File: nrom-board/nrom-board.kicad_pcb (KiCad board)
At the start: 2 copper layers, 90 x 56.8 mm, 12 parts, among them J1 Cartridge Connector, SW1 SW_DIP_x04, SW2 SW_SPDT, U1 PRG ROM 512K, U2 CHR ROM 512K

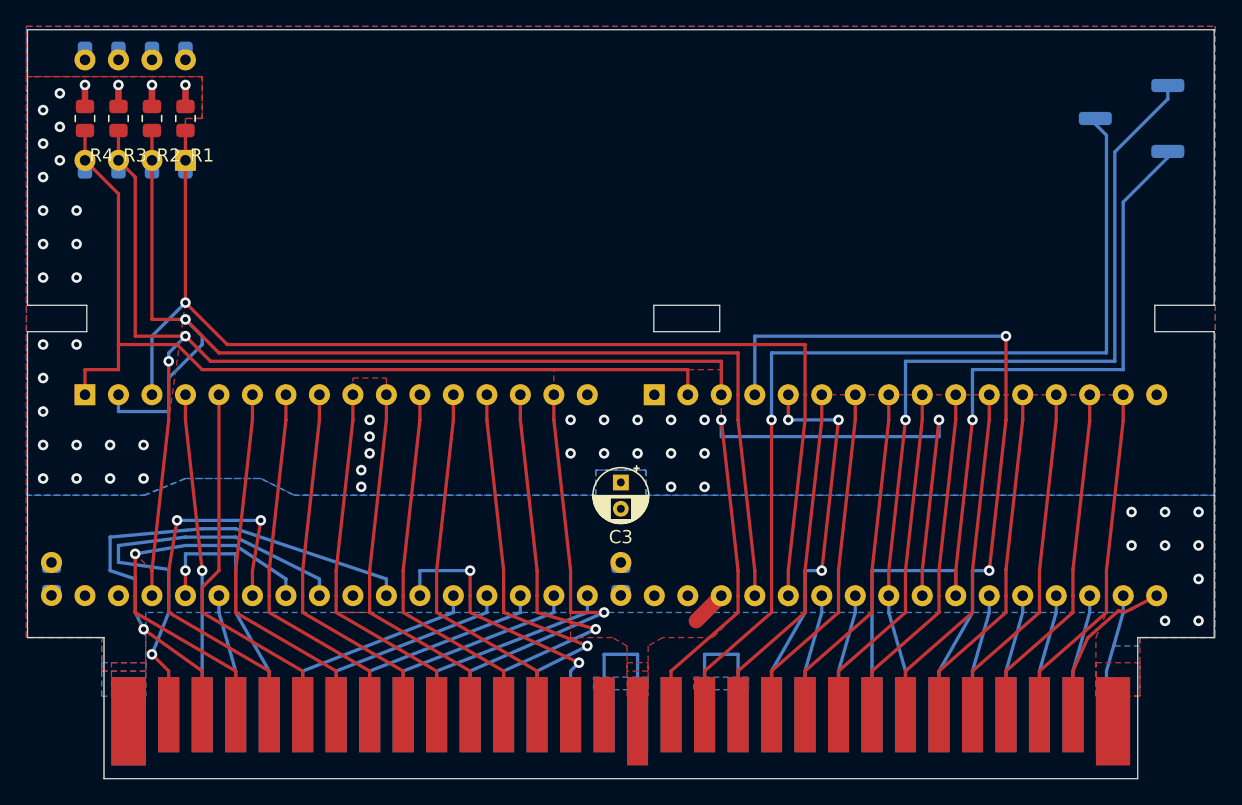
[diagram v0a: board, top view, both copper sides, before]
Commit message: NROM x16: Refactor ROM bankswitching circuit
- Refactor routing
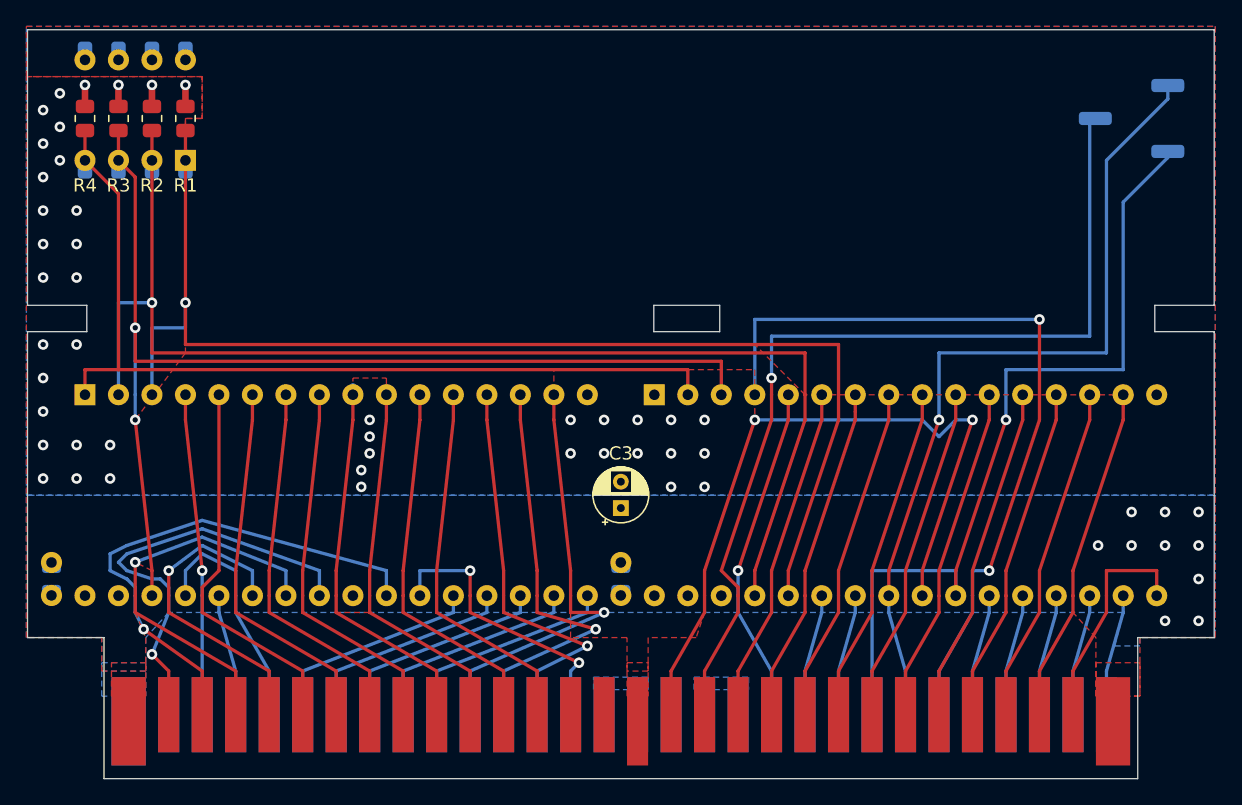
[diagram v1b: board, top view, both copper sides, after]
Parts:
- moved C3 1.95 mm to (63.5, 53.7), turned to 90 degrees
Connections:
- U2 pad 30: GND -> VCC
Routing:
- net /CIRAM_~{CE}: track 11.7 -> 0.00 mm
- net /AUD_2A03: track 11.7 -> 0.00 mm
- net /CPU_A8: track 31.3 -> 24.6 mm, vias 2 -> 1
- net /DIP_0: track 88.5 -> 95.0 mm
- net /PPU_A12: track 54.2 -> 59.8 mm
- net /PPU_D3: track 12.4 -> 17.3 mm
- net /PPU_A7: track 30.1 -> 25.6 mm, vias 3 -> 1
- net /DIP_1: track 92.0 -> 95.0 mm
- net GND: track 9.20 -> 6.51 mm, vias 45 -> 43
- net /PPU_A11: track 65.5 -> 63.1 mm
- net /PPU_~{RD}: track 57.2 -> 55.2 mm
- net /PPU_A10: track 65.8 -> 63.8 mm
- net /CIRAM_A10: track 73.3 -> 71.3 mm
- net /CPU_A14: track 19.9 -> 18.1 mm, vias 1 -> 0
- net /DIP_2: track 84.2 -> 85.4 mm
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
